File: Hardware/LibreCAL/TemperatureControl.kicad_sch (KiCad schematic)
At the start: 9 parts, among them Q1 IRLML2060

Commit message: Partial routing
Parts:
- removed R10, R11: 13, Resistor_SMD:R_2512_6332Metric, symbol Device:R
- R8, R9: value 13 -> 6R2
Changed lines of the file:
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@@
   (junction (at 194.31 92.71) (diameter 0) (color 0 0 0 0)
   )
-  (junction (at 96.52 99.06) (diameter 0) (color 0 0 0 0)
-  )
-  (junction (at 101.6 76.2) (diameter 0) (color 0 0 0 0)
-  )
   (junction (at 170.18 92.71) (diameter 0) (color 0 0 0 0)
   )
@@
     (stroke (width 0) (type default) (color 0 0 0 0))
   )
-  (wire (pts (xy 106.68 76.2) (xy 101.6 76.2))
-    (stroke (width 0) (type default) (color 0 0 0 0))
-  )
-  (wire (pts (xy 96.52 78.74) (xy 96.52 76.2))
+  (wire (pts (xy 96.52 73.66) (xy 96.52 78.74))
     (stroke (width 0) (type default) (color 0 0 0 0))
   )
@@
     (stroke (width 0) (type default) (color 0 0 0 0))
   )
-  (wire (pts (xy 106.68 99.06) (xy 96.52 99.06))
-    (stroke (width 0) (type default) (color 0 0 0 0))
-  )
   (wire (pts (xy 170.18 80.01) (xy 170.18 82.55))
     (stroke (width 0) (type default) (color 0 0 0 0))
@@
     (stroke (width 0) (type default) (color 0 0 0 0))
   )
-  (wire (pts (xy 106.68 96.52) (xy 106.68 99.06))
-    (stroke (width 0) (type default) (color 0 0 0 0))
-  )
-  (wire (pts (xy 96.52 76.2) (xy 101.6 76.2))
-    (stroke (width 0) (type default) (color 0 0 0 0))
-  )
-  (wire (pts (xy 106.68 86.36) (xy 106.68 88.9))
-    (stroke (width 0) (type default) (color 0 0 0 0))
-  )
   (wire (pts (xy 86.36 106.68) (xy 88.9 106.68))
     (stroke (width 0) (type default) (color 0 0 0 0))
   )
-  (wire (pts (xy 96.52 99.06) (xy 96.52 101.6))
-    (stroke (width 0) (type default) (color 0 0 0 0))
-  )
-  (wire (pts (xy 101.6 76.2) (xy 101.6 73.66))
+  (wire (pts (xy 96.52 96.52) (xy 96.52 101.6))
     (stroke (width 0) (type default) (color 0 0 0 0))
   )
@@
     (stroke (width 0) (type default) (color 0 0 0 0))
   )
-  (wire (pts (xy 96.52 96.52) (xy 96.52 99.06))
-    (stroke (width 0) (type default) (color 0 0 0 0))
-  )
   (wire (pts (xy 194.31 102.87) (xy 194.31 105.41))
     (stroke (width 0) (type default) (color 0 0 0 0))
   )
   (wire (pts (xy 191.77 92.71) (xy 194.31 92.71))
-    (stroke (width 0) (type default) (color 0 0 0 0))
-  )
-  (wire (pts (xy 106.68 78.74) (xy 106.68 76.2))
     (stroke (width 0) (type default) (color 0 0 0 0))
   )
@@
     (pin "2")
   )
-  (symbol (lib_id "Device:R") (at 106.68 82.55 0) (unit 1)
-    (in_bom yes) (on_board yes) (fields_autoplaced)
-    (property "Reference" "R10" (id 0) (at 109.22 81.2799 0)
-      (effects (font (size 1.27 1.27)) (justify left))
-    )
-    (property "Value" "13" (id 1) (at 109.22 83.8199 0)
-      (effects (font (size 1.27 1.27)) (justify left))
-    )
-    (property "Footprint" "Resistor_SMD:R_2512_6332Metric" (id 2) (at 104.902 82.55 90)
-      (effects (font (size 1.27 1.27)) hide)
-    )
-    (property "Datasheet" "~" (id 3) (at 106.68 82.55 0)
-      (effects (font (size 1.27 1.27)) hide)
-    )
-    (pin "1")
-    (pin "2")
-  )
-  (symbol (lib_id "Device:R") (at 106.68 92.71 0) (unit 1)
-    (in_bom yes) (on_board yes) (fields_autoplaced)
-    (property "Reference" "R11" (id 0) (at 109.22 91.4399 0)
-      (effects (font (size 1.27 1.27)) (justify left))
-    )
-    (property "Value" "13" (id 1) (at 109.22 93.9799 0)
-      (effects (font (size 1.27 1.27)) (justify left))
-    )
-    (property "Footprint" "Resistor_SMD:R_2512_6332Metric" (id 2) (at 104.902 92.71 90)
-      (effects (font (size 1.27 1.27)) hide)
-    )
-    (property "Datasheet" "~" (id 3) (at 106.68 92.71 0)
-      (effects (font (size 1.27 1.27)) hide)
-    )
-    (pin "1")
-    (pin "2")
-  )
   (symbol (lib_id "Device:R") (at 170.18 86.36 0) (mirror y) (unit 1)
     (in_bom yes) (on_board yes) (fields_autoplaced)
@@
       (effects (font (size 1.27 1.27)) (justify left))
     )
-    (property "Value" "13" (id 1) (at 99.06 93.9799 0)
+    (property "Value" "6R2" (id 1) (at 99.06 93.9799 0)
       (effects (font (size 1.27 1.27)) (justify left))
     )
@@
       (effects (font (size 1.27 1.27)) (justify left))
     )
-    (property "Value" "13" (id 1) (at 99.06 83.8199 0)
+    (property "Value" "6R2" (id 1) (at 99.06 83.8199 0)
       (effects (font (size 1.27 1.27)) (justify left))
     )
@@
     (pin "1")
   )
-  (symbol (lib_id "power:+5V") (at 101.6 73.66 0) (unit 1)
-    (in_bom yes) (on_board yes) (fields_autoplaced)
-    (property "Reference" "#PWR077" (id 0) (at 101.6 77.47 0)
-      (effects (font (size 1.27 1.27)) hide)
-    )
-    (property "Value" "+5V" (id 1) (at 101.6 68.58 0))
-    (property "Footprint" "" (id 2) (at 101.6 73.66 0)
-      (effects (font (size 1.27 1.27)) hide)
-    )
-    (property "Datasheet" "" (id 3) (at 101.6 73.66 0)
-      (effects (font (size 1.27 1.27)) hide)
-    )
+  (symbol (lib_id "power:+5V") (at 96.52 73.66 0) (unit 1)
+    (in_bom yes) (on_board yes) (fields_autoplaced)
+    (property "Reference" "#PWR077" (id 0) (at 96.52 77.47 0)
+      (effects (font (size 1.27 1.27)) hide)
+    )
+    (property "Value" "+5V" (id 1) (at 96.52 68.58 0))
+    (property "Footprint" "" (id 2) (at 96.52 73.66 0)
+      (effects (font (size 1.27 1.27)) hide)
+    )
+    (property "Datasheet" "" (id 3) (at 96.52 73.66 0)
+      (effects (font (size 1.27 1.27)) hide)
+    )

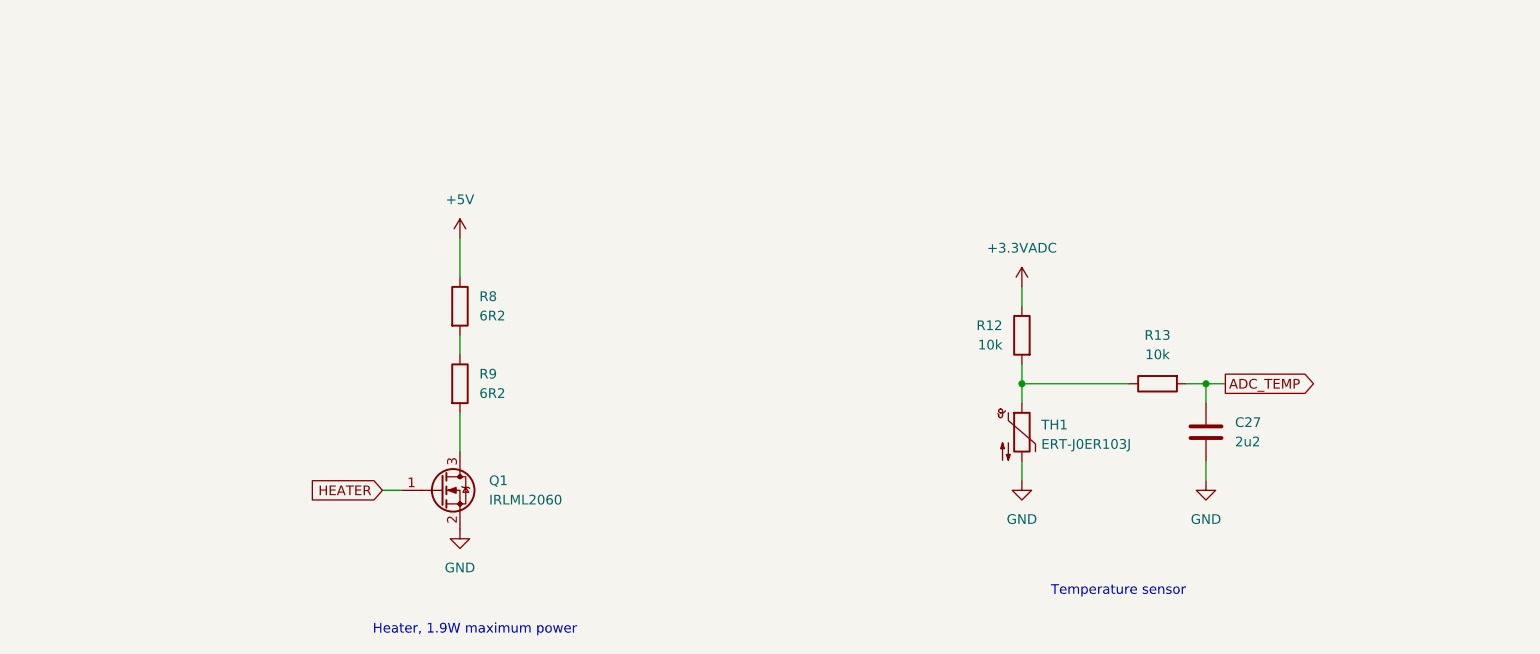
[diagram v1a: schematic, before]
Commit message: Filters added, housing updated
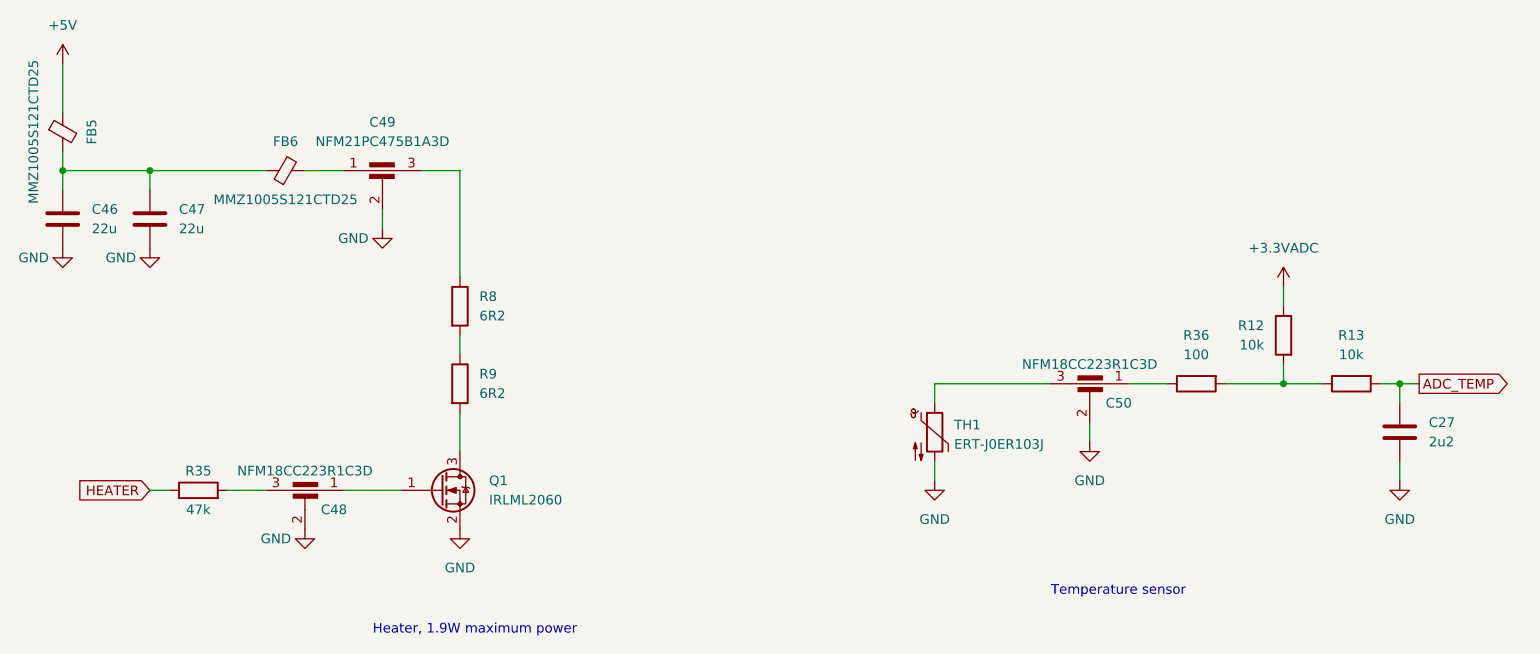
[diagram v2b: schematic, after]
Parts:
- added C46, C47: 22u, Capacitor_SMD:C_0805_2012Metric, symbol Device:C
- added C48, C50: NFM18CC223R1C3D, LibreCAL:NFM18CC, symbol Device:C_Feedthrough
- added C49: NFM21PC475B1A3D, LibreCAL:NFM21PC, symbol Device:C_Feedthrough
- added FB5, FB6: MMZ1005S121CTD25, Inductor_SMD:L_0402_1005Metric, symbol Device:FerriteBead_Small
- added R35: 47k, Resistor_SMD:R_0402_1005Metric, symbol Device:R
- added R36: 100, Resistor_SMD:R_0402_1005Metric, symbol Device:R
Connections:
- net +5V: now also FB5.1; no longer R8.1
- net GND: now also C46.2, C47.2, C48.2, C49.2, C50.2
- net HEATER: now also R35.1; no longer Q1.1 (G)
- net at R12.2, R13.1: now also R36.2; no longer TH1.1
- new net: C48.1, Q1.1 (G)
- new net: C48.3, R35.2
- new net: C46.1, C47.1, FB5.2, FB6.1
- new net: C49.1, FB6.2
- new net: C50.1, R36.1
- new net: C49.3, R8.1
- new net: C50.3, TH1.1
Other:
- moved on the sheet: C27, R12, R13, TH1

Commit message: Improvements on LibreCAL KiCad: fixed minor errors/labels(cosmetic), improved BOM(Added LCSC_Part), improved Impedance JLCPCB 4Layer JLC7628 1.6mm
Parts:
- C27: LCSC_Part (none) -> C307418
- C46, C47: LCSC_Part (none) -> C45783
- C48, C50: LCSC_Part (none) -> C98102
- C49: LCSC_Part (none) -> C96293
- FB5, FB6: LCSC_Part (none) -> C404693
- Q1: LCSC_Part (none) -> C67275
- R12, R13: LCSC_Part (none) -> C723353
- R35: LCSC_Part (none) -> C144757
- R36: LCSC_Part (none) -> C25076
- R8, R9: LCSC_Part (none) -> C147196
- TH1: LCSC_Part (none) -> C153027
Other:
- title: (none) -> LibreCAL
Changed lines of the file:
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@@
 (kicad_sch (version 20211123) (generator eeschema)
   (paper "A4")
+  (title_block
+    (title "LibreCAL")
+    (date "2023-01-07")
+    (rev "A+")
+  )
   (junction (at 55.88 64.77) (diameter 0) (color 0 0 0 0)
   )
@@
       (effects (font (size 1.27 1.27)) hide)
     )
+    (property "LCSC_Part" "C723353" (id 4) (at 213.36 92.71 0)
+      (effects (font (size 1.27 1.27)) hide)
+    )
     (pin "1")
     (pin "2")
@@
       (effects (font (size 1.27 1.27)) hide)
     )
+    (property "LCSC_Part" "C98102" (id 4) (at 76.2 109.22 0)
+      (effects (font (size 1.27 1.27)) hide)
+    )
     (pin "1")
     (pin "2")
@@
       (effects (font (size 1.27 1.27)) hide)
     )
+    (property "LCSC_Part" "C404693" (id 4) (at 44.45 59.69 0)
+      (effects (font (size 1.27 1.27)) hide)
+    )
     (pin "1")
     (pin "2")
@@
     )
     (property "Datasheet" "~" (id 3) (at 204.47 86.36 0)
+      (effects (font (size 1.27 1.27)) hide)
+    )
+    (property "LCSC_Part" "C723353" (id 4) (at 204.47 86.36 0)
       (effects (font (size 1.27 1.27)) hide)
     )
@@
       (effects (font (size 1.27 1.27)) hide)
     )
+    (property "LCSC_Part" "C404693" (id 4) (at 73.66 64.77 0)
+      (effects (font (size 1.27 1.27)) hide)
+    )
     (pin "1")
     (pin "2")
@@
     )
     (property "Datasheet" "~" (id 3) (at 96.52 92.71 0)
+      (effects (font (size 1.27 1.27)) hide)
+    )
+    (property "LCSC_Part" "C147196" (id 4) (at 96.52 92.71 0)
       (effects (font (size 1.27 1.27)) hide)
     )
@@
       (effects (font (size 1.27 1.27)) hide)
     )
+    (property "LCSC_Part" "C25076" (id 4) (at 193.04 92.71 0)
+      (effects (font (size 1.27 1.27)) hide)
+    )
     (pin "1")
     (pin "2")
@@
     )
     (property "Datasheet" "~" (id 3) (at 219.71 99.06 0)
+      (effects (font (size 1.27 1.27)) hide)
+    )
+    (property "LCSC_Part" "C307418" (id 4) (at 219.71 99.06 0)
       (effects (font (size 1.27 1.27)) hide)
     )
@@
       (effects (font (size 1.27 1.27)) hide)
     )
+    (property "LCSC_Part" "C45783" (id 4) (at 44.45 71.12 0)
+      (effects (font (size 1.27 1.27)) hide)
+    )
     (pin "1")
     (pin "2")
@@
     )
     (property "Datasheet" "~" (id 3) (at 96.52 82.55 0)
+      (effects (font (size 1.27 1.27)) hide)
+    )
+    (property "LCSC_Part" "C147196" (id 4) (at 96.52 82.55 0)
       (effects (font (size 1.27 1.27)) hide)
     )
@@
       (effects (font (size 1.27 1.27)) hide)
     )
+    (property "LCSC_Part" "C98102" (id 4) (at 179.07 95.25 0)
+      (effects (font (size 1.27 1.27)) hide)
+    )
     (pin "1")
     (pin "2")
@@
     )
     (property "Datasheet" "~" (id 3) (at 55.88 71.12 0)
+      (effects (font (size 1.27 1.27)) hide)
+    )
+    (property "LCSC_Part" "C45783" (id 4) (at 55.88 71.12 0)
       (effects (font (size 1.27 1.27)) hide)
     )
@@
       (effects (font (size 1.27 1.27)) hide)
     )
+    (property "LCSC_Part" "C96293" (id 4) (at 86.36 67.31 0)
+      (effects (font (size 1.27 1.27)) hide)
+    )
     (pin "1")
     (pin "2")
@@
       (effects (font (size 1.27 1.27)) hide)
     )
+    (property "LCSC_Part" "C144757" (id 4) (at 62.23 106.68 0)
+      (effects (font (size 1.27 1.27)) hide)
+    )
     (pin "1")
     (pin "2")
@@
     )
     (property "Datasheet" "~" (id 3) (at 158.75 97.79 0)
+      (effects (font (size 1.27 1.27)) hide)
+    )
+    (property "LCSC_Part" "C153027" (id 4) (at 158.75 99.06 0)
       (effects (font (size 1.27 1.27)) hide)
     )
@@
       (effects (font (size 1.27 1.27)) (justify left) hide)
     )
-    (pin "1")
+    (property "LCSC_Part" "C67275" (id 4) (at 93.98 106.68 0)
+      (effects (font (size 1.27 1.27)) hide)
+    )
+    (pin "1")
